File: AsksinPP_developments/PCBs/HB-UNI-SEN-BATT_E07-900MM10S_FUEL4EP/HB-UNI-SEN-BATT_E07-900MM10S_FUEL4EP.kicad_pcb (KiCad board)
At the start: 2 copper layers, 75 x 75 mm, 32 parts, among them J1 Conn_01x02, J10 charge, J11 ePaper connector, J12 U.FL connector, J2 Conn_01x02, J3 Conn_01x02, J4 Conn_01x02, J5 ISP Programmer, J6 Conn_01x04, J7 Conn_01x04, J8 Conn_01x04, J9 Conn_01x04, Q1 IRLU024N, SW1 config button

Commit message: PCBs/HB-UNI-SEN-BATT_E07-900MM10S_FUEL4EP: migration to KiCAD 8
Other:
- board text added: "Version 1.1 - 09/2024 (KiCAD 8)"
- board text removed: "Version 1.0 - 09/2023 (KiCAD 6)"

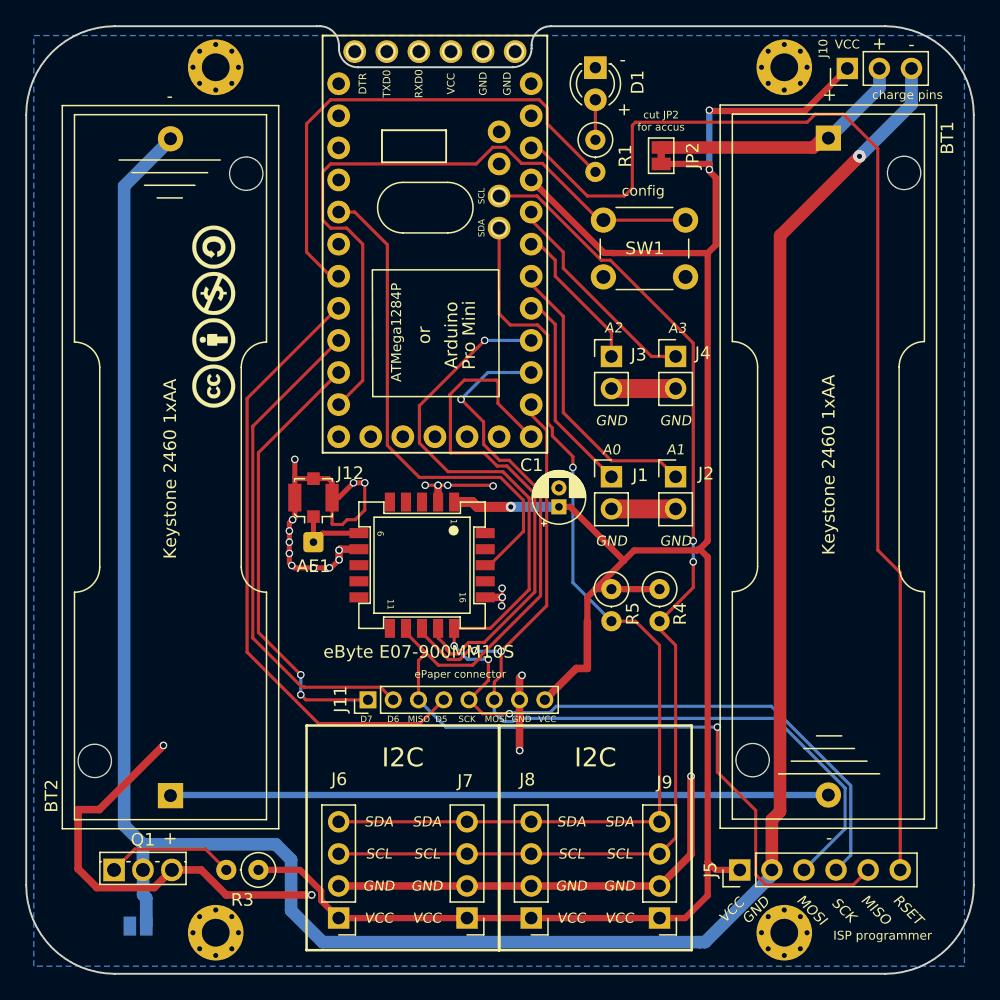
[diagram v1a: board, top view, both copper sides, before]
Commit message: update of PCBs/HB-UNI-SEN-BATT_E07-868MS10_FUEL4EP, PCBs/HB-UNI-SEN-BATT_E07-900M10S_FUEL4EP, and PCBs/HB-UNI-SEN-BATT_E07-900MM10S_FUEL4EP to support HB_Pro_Mini_ATMEGA1284P_FUEL4EP
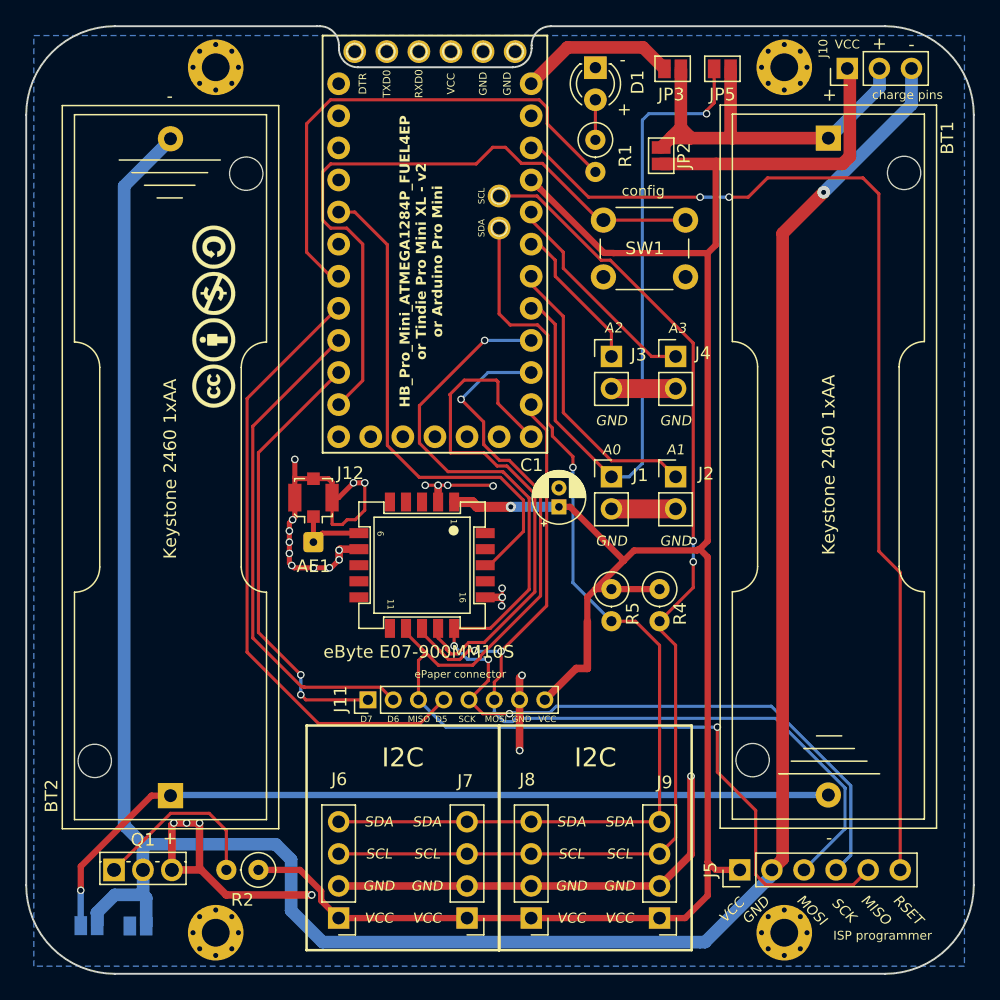
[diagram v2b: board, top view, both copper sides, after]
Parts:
- removed R3: 100K, Resistor_THT:R_Axial_DIN0207_L6.3mm_D2.5mm_P2.54mm_Vertical
- added JP3: internal boost, Jumper:SolderJumper-2_P1.3mm_Open_Pad1.0x1.5mm, F.Cu at (51.2, -71.6)
- added JP4: no BT2 battery, FUEL4EP:SolderJumper-2_P1.3mm_Open_Pad1.0x1.5mm, F.Cu at (4.97, -3.81)
- added JP5: battery voltage measurement, Jumper:SolderJumper-2_P1.3mm_Open_Pad1.0x1.5mm, F.Cu at (55.1, -71.6)
- added R2: 100K, Resistor_THT:R_Axial_DIN0207_L6.3mm_D2.5mm_P2.54mm_Vertical, F.Cu at (18.4, -8.22)
- JP2: value cut for accus -> battery supply; footprint Jumper:SolderJumper-2_P1.3mm_Bridged_Pad1.0x1.5mm -> Jumper:SolderJumper-2_P1.3mm_Open_Pad1.0x1.5mm
- Module2: value Tindie_Pro_Mini_XL_V2 -> HB_Pro_Mini_ATMEGA1284P_FUEL4EP; footprint FUEL4EP:Tindie_ArduinoProMiniXL_1284P_V2 -> FUEL4EP:HB_Pro_Mini_ATMEGA1284P_FUEL4EP
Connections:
- Module2 pad 1A: unconnected-(Module2-VCC-Pad1A) -> /V_ACCU
- Module2 pad 1E: unconnected-(Module2-VCC-Pad1E) -> /SCL
- Module2 pad 2E: GND -> /SDA
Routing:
- net /A0: track 15.7 -> 54.9 mm, vias 0 -> 1
- net /conBAT: track 52.1 -> 66.2 mm, vias 0 -> 1
- net GND: track 124.7 -> 112.1 mm, vias 24 -> 26
- net /V_ACCU: track 0.00 -> 12.4 mm
- net /plusBAT: track 20.8 -> 33.1 mm
- net /RSET: track 92.9 -> 83.9 mm, vias 0 -> 2
- net /minusBAT: track 190.2 -> 195.5 mm
- net Net-(Q1-G): track 10.3 -> 14.4 mm
- net VCC: track 178.7 -> 179.1 mm, vias 3 -> 1
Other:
- board text added: "HB_Pro_Mini_ATMEGA1284P_FUEL4EP or Tindie Pro Mini XL - v2 or Arduino Pro Mini"
- board text added: "JLCJLCJLCJLC"
- board text added: "Version 1.2 - 03/2024 (KiCAD 8)"
- board text removed: "Arduino"
- board text removed: "Pro Mini"
- board text removed: "Version 1.1 - 09/2024 (KiCAD 8)"
- board text removed: "cut JP2 for accus"
- board text removed: "or"
